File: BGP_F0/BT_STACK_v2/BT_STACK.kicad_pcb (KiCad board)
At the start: 2 copper layers, 24 x 26 mm, 19 parts, among them P1 CONN_01X05, P3 CONN_01X04, U1 MC33178

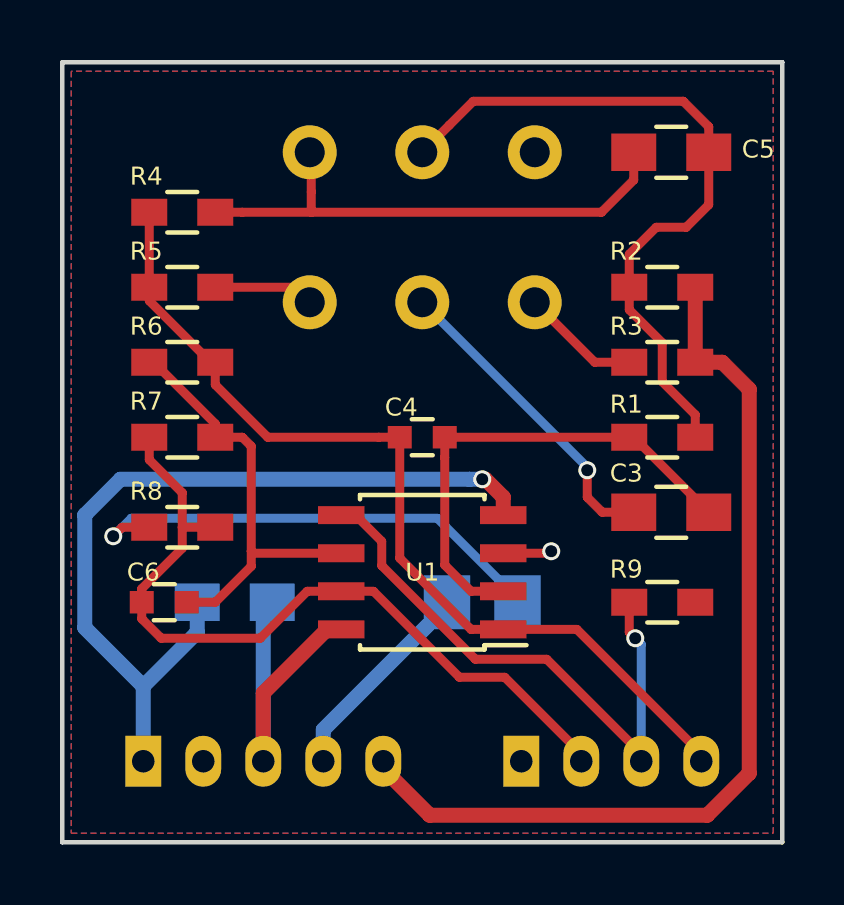
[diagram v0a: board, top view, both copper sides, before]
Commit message: F0 - Boost only - boost/cut bypass
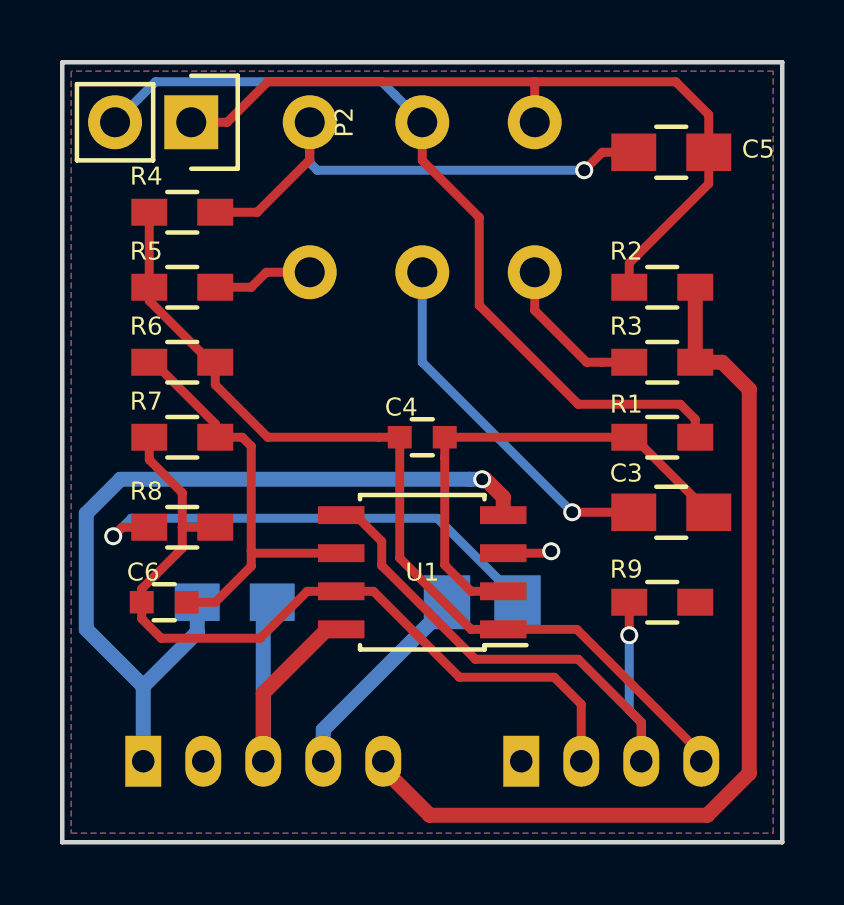
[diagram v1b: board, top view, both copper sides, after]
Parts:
- added P2: CONN_01X02, Pin_Headers:Pin_Header_Straight_1x02, F.Cu at (144.3, 71.0)
- R3, R5: value 1k -> 1.8k
- moved RV1 1.00 mm to (148.2, 71.0)
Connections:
- C5 pad 2: /BW -> /B+
- R2 pad 1: /BW -> /B+
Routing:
- net /B+: track 0.00 -> 26.6 mm
- net /BW: track 23.6 -> 27.6 mm
- net /TW: track 10.5 -> 12.1 mm
- net /T+: track 3.98 -> 5.14 mm
- net /MID_O: track 26.2 -> 27.2 mm
- net /MID_R: track 19.5 -> 20.1 mm
- net /B-: track 17.3 -> 17.6 mm, vias 0 -> 1

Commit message: Slight changes
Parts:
- moved RV1 0.50 mm to (148.2, 71.5)
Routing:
- net /B-: track 17.6 -> 21.0 mm, vias 1 -> 0
- net /T+: track 5.14 -> 6.20 mm
- net /TW: track 12.1 -> 13.0 mm
- net /BW: track 27.6 -> 27.4 mm, vias 0 -> 1
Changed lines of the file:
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@@
     (links 38)
     (no_connects 0)
-    (area 139.924999 68.924999 164.075001 95.075001)
+    (area 139.674999 66.864286 164.085715 95.075001)
     (thickness 1.6)
     (drawings 8)
-    (tracks 142)
+    (tracks 146)
     (zones 0)
     (modules 20)
@@
   )
   (module LIBS:Potentiometer_Alpha_Double_Vertical_Dual_Shaft (layer B.Cu)
-    (at 148.25 71 90)
+    (at 148.25 71.5 90)
     (descr "Potentiometer, vertically mounted, Omeg PC16PU, Omeg PC16PU, Omeg PC16PU, Vishay/Spectrol 248GJ/249GJ Single, Vishay/Spectrol 248GJ/249GJ Single, Vishay/Spectrol 248GJ/249GJ Single, Vishay/Spectrol 248GH/249GH Single, Vishay/Spectrol 148/149 Single, Vishay/Spectrol 148/149 Single, Vishay/Spectrol 148/149 Single, Vishay/Spectrol 148A/149A Single with mounting plates, Vishay/Spectrol 148/149 Double, Vishay/Spectrol 148A/149A Double with mounting plates, Piher PC-16 Single, Piher PC-16 Single, Piher PC-16 Single, Piher PC-16SV Single, Piher PC-16 Double, Piher PC-16 Triple, Piher T16H Single, Piher T16L Single, Piher T16H Double, Alps RK163 Single, Alps RK163 Double, Alps RK097 Single, Alps RK097 Double, http://www.alps.com/prod/info/E/HTML/Potentiometer/RotaryPotentiometers/RK097/RK09712100AV.html")
     (tags "Potentiometer vertical  Omeg PC16PU  Omeg PC16PU  Omeg PC16PU  Vishay/Spectrol 248GJ/249GJ Single  Vishay/Spectrol 248GJ/249GJ Single  Vishay/Spectrol 248GJ/249GJ Single  Vishay/Spectrol 248GH/249GH Single  Vishay/Spectrol 148/149 Single  Vishay/Spectrol 148/149 Single  Vishay/Spectrol 148/149 Single  Vishay/Spectrol 148A/149A Single with mounting plates  Vishay/Spectrol 148/149 Double  Vishay/Spectrol 148A/149A Double with mounting plates  Piher PC-16 Single  Piher PC-16 Single  Piher PC-16 Single  Piher PC-16SV Single  Piher PC-16 Double  Piher PC-16 Triple  Piher T16H Single  Piher T16L Single  Piher T16H Double  Alps RK163 Single  Alps RK163 Double  Alps RK097 Single  Alps RK097 Double Dual Shaft")
-    (fp_text reference RV1 (at -12.3 9.75 180) (layer B.SilkS)
+    (fp_text reference RV1 (at -11.2 9.55 180) (layer B.SilkS)
       (effects (font (size 0.6 0.6) (thickness 0.15)) (justify mirror))
     )
@@
   (segment (start 152.82398 87.12573) (end 148.7 91.24971) (width 0.5) (layer B.Cu) (net 4))
   (segment (start 148.7 91.24971) (end 148.7 92.3) (width 0.5) (layer B.Cu) (net 4))
-  (segment (start 157 84) (end 159.05 84) (width 0.3) (layer F.Cu) (net 5))
-  (segment (start 152 76) (end 152 79) (width 0.3) (layer B.Cu) (net 5))
-  (segment (start 152 79) (end 157 84) (width 0.3) (layer B.Cu) (net 5))
-  (via (at 157 84) (size 0.6) (drill 0.4) (layers F.Cu B.Cu) (net 5))
+  (segment (start 158.95 84.1) (end 158.85 84) (width 0.3) (layer F.Cu) (net 5))
+  (segment (start 157.100001 83.700001) (end 157.4 84) (width 0.3) (layer B.Cu) (net 5))
+  (segment (start 152 78.6) (end 157.100001 83.700001) (width 0.3) (layer B.Cu) (net 5))
+  (segment (start 158.85 84) (end 157.824264 84) (width 0.3) (layer F.Cu) (net 5))
+  (segment (start 152 76.5) (end 152 78.6) (width 0.3) (layer B.Cu) (net 5))
+  (segment (start 157.824264 84) (end 157.4 84) (width 0.3) (layer F.Cu) (net 5))
+  (segment (start 159.05 84) (end 157.4 84) (width 0.3) (layer F.Cu) (net 5))
+  (via (at 157.4 84) (size 0.6) (drill 0.4) (layers F.Cu B.Cu) (net 5))
   (segment (start 154.7 86.635) (end 153.625 86.635) (width 0.3) (layer F.Cu) (net 6))
   (segment (start 153.625 86.635) (end 152.75 85.76) (width 0.3) (layer F.Cu) (net 6))
@@
   (segment (start 145.1 79) (end 144.95 79) (width 0.3) (layer F.Cu) (net 7))
   (segment (start 144.95 79) (end 142.9 76.95) (width 0.3) (layer F.Cu) (net 7))
-  (segment (start 160.449999 69.649999) (end 161.55 70.75) (width 0.3) (layer F.Cu) (net 8))
-  (segment (start 161.55 70.75) (end 161.55 72) (width 0.3) (layer F.Cu) (net 8))
-  (segment (start 155.75 69.649999) (end 160.449999 69.649999) (width 0.3) (layer F.Cu) (net 8))
+  (segment (start 155.75 71.5) (end 155.75 69.65) (width 0.3) (layer F.Cu) (net 8))
+  (segment (start 155.75 69.65) (end 155.8 69.6) (width 0.3) (layer F.Cu) (net 8))
+  (segment (start 146.9 69.6) (end 155.8 69.6) (width 0.3) (layer F.Cu) (net 8))
+  (segment (start 155.8 69.6) (end 160.3 69.6) (width 0.3) (layer F.Cu) (net 8))
   (segment (start 144.3 71) (end 145.5 71) (width 0.3) (layer F.Cu) (net 8))
-  (segment (start 145.5 71) (end 146.850001 69.649999) (width 0.3) (layer F.Cu) (net 8))
-  (segment (start 146.850001 69.649999) (end 155.75 69.649999) (width 0.3) (layer F.Cu) (net 8))
-  (segment (start 155.75 69.649999) (end 155.75 71) (width 0.3) (layer F.Cu) (net 8))
+  (segment (start 145.5 71) (end 146.9 69.6) (width 0.3) (layer F.Cu) (net 8))
+  (segment (start 161.55 70.85) (end 161.55 72) (width 0.3) (layer F.Cu) (net 8))
+  (segment (start 160.3 69.6) (end 161.55 70.85) (width 0.3) (layer F.Cu) (net 8))
   (segment (start 158.9 75.7) (end 161.55 73.05) (width 0.3) (layer F.Cu) (net 8))
   (segment (start 161.55 73.05) (end 161.55 72) (width 0.3) (layer F.Cu) (net 8))
   (segment (start 158.9 76.5) (end 158.9 75.7) (width 0.3) (layer F.Cu) (net 8))
-  (segment (start 161.425 72) (end 161.55 72) (width 0.3) (layer F.Cu) (net 8))
-  (segment (start 145.1 74) (end 146.5 74) (width 0.3) (layer F.Cu) (net 9))
-  (segment (start 146.5 74) (end 148.25 72.25) (width 0.3) (layer F.Cu) (net 9))
+  (segment (start 159.05 72) (end 157.8 72) (width 0.3) (layer F.Cu) (net 9))
+  (segment (start 156.5 73.3) (end 148.25 73.3) (width 0.3) (layer F.Cu) (net 9))
+  (segment (start 157.8 72) (end 156.5 73.3) (width 0.3) (layer F.Cu) (net 9))
+  (segment (start 148.25 73.3) (end 148.25 71.5) (width 0.3) (layer F.Cu) (net 9))
+  (segment (start 148.25 71.5) (end 148.25 73.35) (width 0.3) (layer F.Cu) (net 9))
+  (segment (start 146 74) (end 145.1 74) (width 0.3) (layer F.Cu) (net 9))
+  (segment (start 148.25 73.35) (end 147.6 74) (width 0.3) (layer F.Cu) (net 9))
+  (segment (start 147.6 74) (end 146 74) (width 0.3) (layer F.Cu) (net 9))
   (segment (start 148.25 72.25) (end 148.25 71) (width 0.3) (layer F.Cu) (net 9))
-  (segment (start 157.4 72.6) (end 148.5 72.6) (width 0.3) (layer B.Cu) (net 9))
-  (segment (start 148.5 72.6) (end 148.25 72.35) (width 0.3) (layer B.Cu) (net 9))
   (segment (start 148.25 72.35) (end 148.25 71) (width 0.3) (layer B.Cu) (net 9))
-  (segment (start 159.05 72) (end 158 72) (width 0.3) (layer F.Cu) (net 9))
-  (segment (start 158 72) (end 157.4 72.6) (width 0.3) (layer F.Cu) (net 9))
-  (via (at 157.4 72.6) (size 0.6) (drill 0.4) (layers F.Cu B.Cu) (net 9))
   (segment (start 154.7 85.365) (end 156.235 85.365) (width 0.3) (layer F.Cu) (net 10))
   (segment (start 156.235 85.365) (end 156.3 85.3) (width 0.3) (layer F.Cu) (net 10))
@@
   (segment (start 153.771458 88.9) (end 157.2 88.9) (width 0.3) (layer F.Cu) (net 12))
   (segment (start 159.3 91) (end 159.3 92.3) (width 0.3) (layer F.Cu) (net 12))
-  (segment (start 141.76 71) (end 143.110001 69.649999) (width 0.3) (layer B.Cu) (net 13))
-  (segment (start 151.100001 70.100001) (end 152 71) (width 0.3) (layer B.Cu) (net 13))
-  (segment (start 143.110001 69.649999) (end 150.649999 69.649999) (width 0.3) (layer B.Cu) (net 13))
-  (segment (start 150.649999 69.649999) (end 151.100001 70.100001) (width 0.3) (layer B.Cu) (net 13))
+  (segment (start 161.1 80.3) (end 161.1 81.5) (width 0.3) (layer F.Cu) (net 13))
+  (segment (start 152 71.5) (end 153.272792 71.5) (width 0.3) (layer B.Cu) (net 13))
+  (segment (start 153.272792 71.5) (end 161.1 79.327208) (width 0.3) (layer B.Cu) (net 13))
+  (segment (start 161.1 79.327208) (end 161.1 80.3) (width 0.3) (layer B.Cu) (net 13))
+  (via (at 161.1 80.3) (size 0.6) (drill 0.4) (layers F.Cu B.Cu) (net 13))
+  (segment (start 141.76 71) (end 143.16 69.6) (width 0.3) (layer B.Cu) (net 13))
+  (segment (start 143.16 69.6) (end 150.1 69.6) (width 0.3) (layer B.Cu) (net 13))
+  (segment (start 150.1 69.6) (end 151.100001 70.600001) (width 0.3) (layer B.Cu) (net 13))
+  (segment (start 151.100001 70.600001) (end 152 71.5) (width 0.3) (layer B.Cu) (net 13))
   (segment (start 152 71) (end 152 72.272792) (width 0.3) (layer F.Cu) (net 13))
-  (segment (start 153.9 77.1) (end 157.2 80.4) (width 0.3) (layer F.Cu) (net 13))
-  (segment (start 152 72.272792) (end 153.9 74.172792) (width 0.3) (layer F.Cu) (net 13))
-  (segment (start 153.9 74.172792) (end 153.9 77.1) (width 0.3) (layer F.Cu) (net 13))
-  (segment (start 161.1 80.9) (end 161.1 81.5) (width 0.3) (layer F.Cu) (net 13))
-  (segment (start 157.2 80.4) (end 160.6 80.4) (width 0.3) (layer F.Cu) (net 13))
-  (segment (start 160.6 80.4) (end 161.1 80.9) (width 0.3) (layer F.Cu) (net 13))
-  (segment (start 148.25 76) (end 146.8 76) (width 0.3) (layer F.Cu) (net 14))
-  (segment (start 146.3 76.5) (end 145.1 76.5) (width 0.3) (layer F.Cu) (net 14))
-  (segment (start 146.8 76) (end 146.3 76.5) (width 0.3) (layer F.Cu) (net 14))
+  (segment (start 148.25 76.5) (end 146.977208 76.5) (width 0.3) (layer F.Cu) (net 14))
+  (segment (start 146.977208 76.5) (end 145.1 76.5) (width 0.3) (layer F.Cu) (net 14))
+  (segment (start 155.75 76.5) (end 155.75 77.772792) (width 0.3) (layer F.Cu) (net 15))
+  (segment (start 155.75 77.772792) (end 156.977208 79) (width 0.3) (layer F.Cu) (net 15))
+  (segment (start 156.977208 79) (end 158 79) (width 0.3) (layer F.Cu) (net 15))
+  (segment (start 158 79) (end 158.9 79) (width 0.3) (layer F.Cu) (net 15))
   (segment (start 155.75 76) (end 155.75 77.272792) (width 0.3) (layer F.Cu) (net 15))
-  (segment (start 155.75 77.272792) (end 157.477208 79) (width 0.3) (layer F.Cu) (net 15))
-  (segment (start 157.477208 79) (end 158 79) (width 0.3) (layer F.Cu) (net 15))
-  (segment (start 158 79) (end 158.9 79) (width 0.3) (layer F.Cu) (net 15))
   (segment (start 142.9 79) (end 143.05 79) (width 0.3) (layer F.Cu) (net 16))
   (segment (start 145.1 81.05) (end 145.1 81.5) (width 0.3) (layer F.Cu) (net 16))

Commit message: Slight changes
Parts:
- C4, C6: footprint Capacitors_SMD:C_0603 -> Capacitors_SMD:C_0603_HandSoldering
- moved C6 0.45 mm to (143.8, 87.0)
- moved P2 0.30 mm to (144.0, 71.0)
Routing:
- net /MID_O: track 27.2 -> 26.6 mm

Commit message: F0 BT Layout
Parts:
- P2: footprint Pin_Headers:Pin_Header_Straight_1x02 -> Pin_Headers:Pin_Header_Straight_1x02_Pitch2.54mm; moved to B.Cu
- moved R7 5.30 mm to (149.3, 81.5)
- moved C4 2.70 mm to (154.7, 81.5)
- moved R4 2.50 mm to (144.0, 76.5)
- moved R5 2.50 mm to (144.0, 79.0)
- moved R6 2.50 mm to (144.0, 81.5)
- moved P2 1.24 mm to (142.8, 70.7), turned to 180 degrees
- turned C6 to 180 degrees
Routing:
- net Net-(C6-Pad2): track 14.2 -> 25.2 mm, vias 0 -> 2
- net /MID_I: track 30.6 -> 34.4 mm
- net /MID_O: track 26.6 -> 23.0 mm
- net /BW: track 27.7 -> 25.7 mm
- net Net-(C3-Pad2): track 16.1 -> 14.1 mm
- net Net-(C2-Pad1): track 16.3 -> 14.4 mm
- net /T-: track 3.15 -> 4.80 mm
- net /B-: track 21.0 -> 19.6 mm
- net Earth: track 27.8 -> 26.9 mm
- net /Vref: track 1.63 -> 2.53 mm, vias 1 -> 2
- net /B+: track 27.3 -> 28.2 mm
- net /TW: track 13.0 -> 12.3 mm
